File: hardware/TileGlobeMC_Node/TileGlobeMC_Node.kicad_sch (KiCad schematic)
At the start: 85 parts, among them J1 Conn_01x05, J10 LCD, J2 Conn_01x05, J3 Conn_01x05, J4 Conn_01x05, J5 Conn_01x05, J6 Conn_01x05, J7 Conn_01x05, J8 Conn_01x05, J9 SWD, Q1 2N7002, Q2 2N7002, U1 RP2350_80QFN, U2 TPS62A01DRL, U3 BQ24232RGT, U4 ESP-PSRAM64H, U5 PY25Q128HA-WXH, U6 PY25Q128HA-SSH, U7 74AHC1G04, U8 74AHC1G32, Y1 12M

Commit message: Commit before switching to multi board design
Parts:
- removed U8: 74AHC1G32, Package_TO_SOT_SMD:SOT-23-5, symbol 74xGxx:74AHC1G32
- added C29, C30, C31, C32, C33, C34: 100n, Capacitor_SMD:C_0402_1005Metric, symbol Device:C_Small
- added D1, D2, D4: 1N4148WT, Diode_SMD:D_SOD-523, symbol Diode:1N4148WT
- added D3, D5: 3V, Diode_SMD:D_SOD-523, symbol Device:D_Zener_Small
- added J11: USB_C, Connector_USB:USB_C_Receptacle_GCT_USB4105-xx-A_16P_TopMnt_Horizontal, symbol Connector:USB_C_Receptacle_USB2.0_16P
- added R32, R33: 5.1k, Capacitor_SMD:C_0402_1005Metric, symbol Device:R_Small
- added R34: 100k, Capacitor_SMD:C_0402_1005Metric, symbol Device:R_Small
- added R35, R36, R37, R38, R39, R40, R41: 10k, Capacitor_SMD:C_0402_1005Metric, symbol Device:R_Small
- added SW1, SW2, SW3, SW4, SW5: Left, Button_Switch_SMD:SW_SPST_PTS647_Sx38, symbol Switch:SW_Push
- added U8: SC7A20, Package_LGA:LGA-12_2x2mm_P0.5mm, symbol Sensor_Motion:SC7A20
- J2, J4, J6, J8: value Conn_01x05 -> P_Male; footprint (none) -> Project:BC-15-5P380; symbol Connector_Generic:Conn_01x05 -> Connector_Generic_MountingPin:Conn_01x05_MountingPin
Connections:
- net +5V is gone; now on net VIN: J1.5 (Pin_5), J2.1 (Pin_1), J3.5 (Pin_5), J4.1 (Pin_1), J5.5 (Pin_5), J6.1 (Pin_1), J7.5 (Pin_5), J8.1 (Pin_1)
- net +3V3: now also C29.1, R36.2, R37.2, SW2.2, SW3.2, SW4.2, SW5.2, U8.3 (VDDIO), U8.7 (VDD)
- net 3V3_EN_LATCH: now also D4.2 (A)
- net GND: now also J2.MP (MountPin), J4.MP (MountPin), J6.MP (MountPin), J8.MP (MountPin), C29.2, C30.2, C31.2, C32.2, C33.2, C34.2, D3.2 (A), D5.2 (A), J11.A1 (GND), J11.A12 (GND), J11.B1 (GND), J11.B12 (GND), J11.S1 (SHIELD), R32.1, R33.1, R34.1, U8.4 (NC), U8.8 (GNDIO), U8.9 (GND)
- net USB_D+: now also J11.A6 (D+), J11.B6 (D+)
- net USB_D-: now also J11.A7 (D-), J11.B7 (D-)
- net VBUS: now also SW1.2
- net VIN: now also J11.A4 (VBUS), J11.A9 (VBUS), J11.B4 (VBUS), J11.B9 (VBUS)
- net VIN_PGOOD: now also D2.2 (A)
- net at R23.2: now also D5.1 (K)
- net 3V3_EN: no longer names the net of U2.4 (EN)
- net 3V3_EN: now also D1.1 (K), D2.1 (K), D4.1 (K), R34.2
- net BAT_ISET_SAMPLE renamed BAT_ICHG_SAMPLE
- net VIN_~{PGOOD}: no longer names the net of R22.2, U3.7 (PGOOD), U7.2
- new net: R38.1, SW2.1
- new net: J11.A5 (CC1), R33.2
- new net: J11.B5 (CC2), R32.2
- new net: R41.1, SW5.1
- new net: R39.1, SW3.1
- new net: R40.1, SW4.1
- new net BTN_BOTTOM: C32.1, R39.2
- new net BTN_CENTER: C30.1, D3.1 (K), R35.2
- new net BTN_CENTER_VBUS: D1.2 (A), R35.1, SW1.1
- new net BTN_LEFT: C31.1, R38.2
- new net BTN_RIGHT: C33.1, R40.2
- new net BTN_TOP: C34.1, R41.2
- new net I2C_SCL: U8.12 (SCx)
- new net I2C_SDA: U8.2 (SDx)
- no-connect marks 3 -> 10
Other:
- added sheet Core (Core.kicad_sch)
- added sheet Peripheral (Peripheral.kicad_sch)
- added sheet Power (Power.kicad_sch)
- note added: "3.3V DC-DC"
- note added: "Battery Charger & Power Path"
- note added: "Buttons"
- note added: "Flash & PSRAM"
- note added: "IMU"
- note added: "LCD"
- note added: "Node Ports"
- note added: "Note: buttons use MCU's internal pull-down."
- note added: "TODO: change setting resistors now that we're using bigger batteries"
- note added: "USB-C"
- moved on the sheet: BT1, C25, C26, C27, C28, C4, C5, C7, C8, J1, J10, J3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

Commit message: PCB progress
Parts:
- removed BT1: LIR2032, symbol Device:Battery_Cell
- removed C1, C12, C2, C27, C3, C4, C5, C6, C7, C9: 4.7u, Capacitor_SMD:C_0402_1005Metric, symbol Device:C_Small
- removed C10, C11, C13, C14, C15, C16, C17, C18, C19, C20, C21, C22, C25, C26, C28, C29, C30, C31, C32, C33, C34: 100n, Capacitor_SMD:C_0402_1005Metric, symbol Device:C_Small
- removed C23, C24: 15p, Capacitor_SMD:C_0402_1005Metric, symbol Device:C_Small
- removed C8: 22u, Capacitor_SMD:C_0603_1608Metric, symbol Device:C_Small
- removed D1, D2, D4: 1N4148WT, Diode_SMD:D_SOD-523, symbol Diode:1N4148WT
- removed D3, D5: 3V, Diode_SMD:D_SOD-523, symbol Device:D_Zener_Small
- removed J1, J3, J5, J7: Conn_01x05, symbol Connector_Generic:Conn_01x05
- removed J10: LCD, Connector_FFC-FPC:TE_1-1734839-2_1x12-1MP_P0.5mm_Horizontal, symbol Connector_Generic_MountingPin:Conn_01x12_MountingPin
- removed J11: USB_C, Connector_USB:USB_C_Receptacle_GCT_USB4105-xx-A_16P_TopMnt_Horizontal, symbol Connector:USB_C_Receptacle_USB2.0_16P
- removed J2, J4, J6, J8: P_Male, Project:BC-15-5P380, symbol Connector_Generic_MountingPin:Conn_01x05_MountingPin
- removed J9: SWD, Connector_JST:JST_SH_BM03B-SRSS-TB_1x03-1MP_P1.00mm_Vertical, symbol Connector_Generic_MountingPin:Conn_01x03_MountingPin
- removed JP1: RESET, TestPoint:TestPoint_2Pads_Pitch2.54mm_Drill0.8mm, symbol Jumper:Jumper_2_Small_Open
- removed JP2: USB_BOOT, TestPoint:TestPoint_2Pads_Pitch2.54mm_Drill0.8mm, symbol Jumper:Jumper_2_Small_Open
- removed L1: 3.3u, RP2350:L_pol_2016, symbol Project:L_Polarized_Ferrite_Small
- removed L2: 1u, Inductor_SMD:L_Wuerth_MAPI-2010, symbol Device:L_Ferrite_Small
- removed Q1, Q2: 2N7002, Package_TO_SOT_SMD:SOT-23, symbol Transistor_FET:2N7002
- removed R1, R10, R4, R7: 300, Capacitor_SMD:C_0402_1005Metric, symbol Device:R_Small
- removed R11, R12, R2, R3, R5, R6, R8, R9: 270, Capacitor_SMD:C_0402_1005Metric, symbol Device:R_Small
- removed R13, R24: 33, Capacitor_SMD:C_0402_1005Metric, symbol Device:R_Small
- removed R14, R35, R36, R37, R38, R39, R40, R41: 10k, Capacitor_SMD:C_0402_1005Metric, symbol Device:R_Small
- removed R15: 17.4k, Capacitor_SMD:C_0402_1005Metric, symbol Device:R_Small
- removed R16: 1.5k, Capacitor_SMD:C_0402_1005Metric, symbol Device:R_Small
- removed R17, R18, R19, R22, R23, R28, R29, R34: 100k, Capacitor_SMD:C_0402_1005Metric, symbol Device:R_Small
- removed R20: 86.6k, Capacitor_SMD:C_0402_1005Metric, symbol Device:R_Small
- removed R21: 390k, Capacitor_SMD:C_0402_1005Metric, symbol Device:R_Small
- removed R25, R30: 1k, Capacitor_SMD:C_0402_1005Metric, symbol Device:R_Small
- removed R26, R27: 27, Capacitor_SMD:C_0402_1005Metric, symbol Device:R_Small
- removed R31: 4.7, Capacitor_SMD:C_0402_1005Metric, symbol Device:R_Small
- removed R32, R33: 5.1k, Capacitor_SMD:C_0402_1005Metric, symbol Device:R_Small
- removed SW1, SW2, SW3, SW4, SW5: Left, Button_Switch_SMD:SW_SPST_PTS647_Sx38, symbol Switch:SW_Push
- removed U1: RP2350_80QFN, RP2350:RP2350-QFN-80-1EP_10x10_P0.4mm_EP3.4x3.4mm_ThermalVias, symbol RP2350:RP2350_80QFN
- removed U2: TPS62A01DRL, Package_TO_SOT_SMD:SOT-563, symbol Regulator_Switching:TPS62A01DRL
- removed U3: BQ24232RGT, Package_DFN_QFN:VQFN-16-1EP_3x3mm_P0.5mm_EP1.68x1.68mm_ThermalVias, symbol Project:BQ24232RGT
- removed U4: ESP-PSRAM64H, Package_SO:SOIC-8_3.9x4.9mm_P1.27mm, symbol Project:ESP-PSRAM64
- removed U5: PY25Q128HA-WXH, Package_SON:WSON-8-1EP_6x5mm_P1.27mm_EP3.4x4.3mm, symbol Memory_Flash:W25Q128JVP
- removed U6: PY25Q128HA-SSH, Package_SO:SOIC-8_5.3x5.3mm_P1.27mm, symbol Memory_Flash:W25Q128JVS
- removed U7: 74AHC1G04, Package_TO_SOT_SMD:SOT-23-5, symbol 74xGxx:74AHC1G04
- removed U8: SC7A20, Package_LGA:LGA-12_2x2mm_P0.5mm, symbol Sensor_Motion:SC7A20
- removed Y1: 12M, Crystal:Crystal_SMD_3225-4Pin_3.2x2.5mm, symbol Device:Crystal_GND24
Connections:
- no-connect marks 10 -> 29
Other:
- removed sheet Power
- sheet Core ports: added +3V3, BTN_CENTER, BTN_CENTER_VBUS, GND_CORE, GPIO0, GPIO1, GPIO2, GPIO3, GPIO4, I2C_SCL, I2C_SDA, LCD_CS, LCD_DC, LCD_MOSI, LCD_SCK, PERI_INT, VBUS; removed none
- sheet Peripheral ports: added +3V3, BTN_CENTER, BTN_CENTER_VBUS, GND_PERI, I2C_SCL, I2C_SDA, LCD_CS, LCD_DC, LCD_MOSI, LCD_SCK, PERI_INT, VBUS; removed none
- note removed: "3.3V DC-DC"
- note removed: "Battery Charger & Power Path"
- note removed: "Buttons"
- note removed: "Flash & PSRAM"
- note removed: "IMU"
- note removed: "LCD"
- note removed: "Node Ports"
- note removed: "Note: buttons use MCU's internal pull-down."
- note removed: "TODO: change setting resistors now that we're using bigger batteries"
- note removed: "USB-C"

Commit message: PCB progress
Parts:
- added J20: Conn_01x24_MountingPin, Project:FPC_Verticle_24pin_0.5mm, symbol Connector_Generic_MountingPin:Conn_01x24_MountingPin
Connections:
- no-connect marks 29 -> 35
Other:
- sheet Core ports: added GPIO10, GPIO11, GPIO12, GPIO5, GPIO6, GPIO7, GPIO8, GPIO9, USB_D+, USB_D-, VIN; removed BTN_CENTER, I2C_SCL, I2C_SDA, LCD_CS, LCD_DC, LCD_MOSI, LCD_SCK, PERI_INT
- sheet Peripheral ports: added USB_D+, USB_D-, VIN; removed none

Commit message: Main PCB progress
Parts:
- added J21: Conn_01x24_MountingPin, Project:FPC_Verticle_24pin_0.5mm, symbol Connector_Generic_MountingPin:Conn_01x24_MountingPin
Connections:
- net Core/BTN_CENTER_VBUS: now also J20.23 (Pin_23)
- net Core/GPIO0: now also J20.19 (Pin_19)
- net Core/GPIO1: now also J20.18 (Pin_18)
- net Core/GPIO10: now also J20.9 (Pin_9)
- net Core/GPIO11: now also J20.8 (Pin_8)
- net Core/GPIO12: now also J20.7 (Pin_7)
- net Core/GPIO2: now also J20.17 (Pin_17)
- net Core/GPIO3: now also J20.16 (Pin_16)
- net Core/GPIO4: now also J20.15 (Pin_15)
- net Core/GPIO5: now also J20.14 (Pin_14)
- net Core/GPIO6: now also J20.13 (Pin_13)
- net Core/GPIO7: now also J20.12 (Pin_12)
- net Core/GPIO8: now also J20.11 (Pin_11)
- net Core/GPIO9: now also J20.10 (Pin_10)
- net Core/USB_D+: now also J20.3 (Pin_3)
- net Core/USB_D-: now also J20.2 (Pin_2)
- net Core/VBUS: now also J20.22 (Pin_22)
- net Core/VIN: now also J20.20 (Pin_20), J20.21 (Pin_21)
- net Peripheral/BTN_CENTER_VBUS: now also J21.23 (Pin_23)
- net Peripheral/VBUS: now also J21.22 (Pin_22)
- net Peripheral/VIN: now also J21.20 (Pin_20), J21.21 (Pin_21)
- net GND_CORE: now reaches J20.1 (Pin_1)
- net GND_CORE: now also J20.24 (Pin_24), J20.MP (MountPin)
- new net GND_PERI: J21.1 (Pin_1), J21.24 (Pin_24), J21.MP (MountPin)
- no-connect marks 35 -> 14
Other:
- moved on the sheet: J20

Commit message: Main PCB done
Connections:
- net Core/+3V3: now also J20.5 (Pin_5)
- net GND_CORE: now also J20.4 (Pin_4), J20.6 (Pin_6)
- net GND_PERI: now also J21.4 (Pin_4), J21.6 (Pin_6)
- net Peripheral/+3V3: now also J21.5 (Pin_5)
- net Peripheral/USB_D+: now also J21.3 (Pin_3)
- net Peripheral/USB_D-: now also J21.2 (Pin_2)
- no-connect marks 14 -> 0

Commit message: PCB done
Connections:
- net Peripheral/BTN_CENTER: now also J21.8 (Pin_8)
- net Peripheral/I2C_SCL: now also J21.13 (Pin_13)
- net Peripheral/I2C_SDA: now also J21.14 (Pin_14)
- net Peripheral/LCD_CS: now also J21.19 (Pin_19)
- net Peripheral/LCD_DC: now also J21.16 (Pin_16)
- net Peripheral/LCD_MOSI: now also J21.17 (Pin_17)
- net Peripheral/LCD_SCK: now also J21.18 (Pin_18)
- net Peripheral/PERI_INT: now also J21.15 (Pin_15)
- no-connect marks 0 -> 5
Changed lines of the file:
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@@
 		(color 0 0 0 0)
 	)
+	(no_connect
+		(at 182.88 101.6)
+	)
+	(no_connect
+		(at 182.88 99.06)
+	)
+	(no_connect
+		(at 182.88 93.98)
+	)
+	(no_connect
+		(at 182.88 106.68)
+	)
+	(no_connect
+		(at 182.88 104.14)
+	)
 	(wire
 		(pts
@@
 	(wire
 		(pts
+			(xy 182.88 124.46) (xy 187.96 124.46)
+		)
+		(stroke
+			(width 0)
+			(type default)
+		)
+	)
+	(wire
+		(pts
 			(xy 162.56 109.22) (xy 167.64 109.22)
 		)
@@
 	(wire
 		(pts
+			(xy 182.88 121.92) (xy 187.96 121.92)
+		)
+		(stroke
+			(width 0)
+			(type default)
+		)
+	)
+	(wire
+		(pts
 			(xy 162.56 81.28) (xy 167.64 81.28)
 		)
@@
 	(wire
 		(pts
+			(xy 182.88 119.38) (xy 187.96 119.38)
+		)
+		(stroke
+			(width 0)
+			(type default)
+		)
+	)
+	(wire
+		(pts
 			(xy 182.88 129.54) (xy 187.96 129.54)
 		)
@@
 	(wire
 		(pts
+			(xy 182.88 96.52) (xy 187.96 96.52)
+		)
+		(stroke
+			(width 0)
+			(type default)
+		)
+	)
+	(wire
+		(pts
 			(xy 162.56 124.46) (xy 167.64 124.46)
 		)
@@
 	(wire
 		(pts
+			(xy 182.88 109.22) (xy 187.96 109.22)
+		)
+		(stroke
+			(width 0)
+			(type default)
+		)
+	)
+	(wire
+		(pts
 			(xy 162.56 104.14) (xy 167.64 104.14)
 		)
@@
 	(wire
 		(pts
+			(xy 182.88 114.3) (xy 187.96 114.3)
+		)
+		(stroke
+			(width 0)
+			(type default)
+		)
+	)
+	(wire
+		(pts
 			(xy 162.56 119.38) (xy 167.64 119.38)
 		)
@@
 	(wire
 		(pts
+			(xy 182.88 116.84) (xy 187.96 116.84)
+		)
+		(stroke
+			(width 0)
+			(type default)
+		)
+	)
+	(wire
+		(pts
 			(xy 162.56 111.76) (xy 167.64 111.76)
+		)
+		(stroke
+			(width 0)
+			(type default)
+		)
+	)
+	(wire
+		(pts
+			(xy 182.88 111.76) (xy 187.96 111.76)
 		)
 		(stroke
@@
 		)
 		(pin "BTN_CENTER" output
-			(at 187.96 92.71 180)
+			(at 187.96 96.52 180)
 			(effects
 				(font
@@
 		)
 		(pin "I2C_SCL" input
-			(at 187.96 96.52 180)
+			(at 187.96 109.22 180)
 			(effects
 				(font
@@
 		)
 		(pin "I2C_SDA" bidirectional
-			(at 187.96 99.06 180)
+			(at 187.96 111.76 180)
 			(effects
 				(font
@@
 		)
 		(pin "LCD_CS" input
-			(at 187.96 104.14 180)
+			(at 187.96 124.46 180)
 			(effects
 				(font
@@
 		)
 		(pin "LCD_DC" input
-			(at 187.96 106.68 180)
+			(at 187.96 116.84 180)
 			(effects
 				(font
@@
 		)
 		(pin "LCD_MOSI" input
-			(at 187.96 110.49 180)
+			(at 187.96 119.38 180)
 			(effects
 				(font
@@
 		)
 		(pin "LCD_SCK" input
-			(at 187.96 113.03 180)
+			(at 187.96 121.92 180)
 			(effects
 				(font
@@
 		)
 		(pin "PERI_INT" output
-			(at 187.96 118.11 180)
-			(effects
-				(font
+			(at 187.96 114.3 180)
+			(effects
+				(font

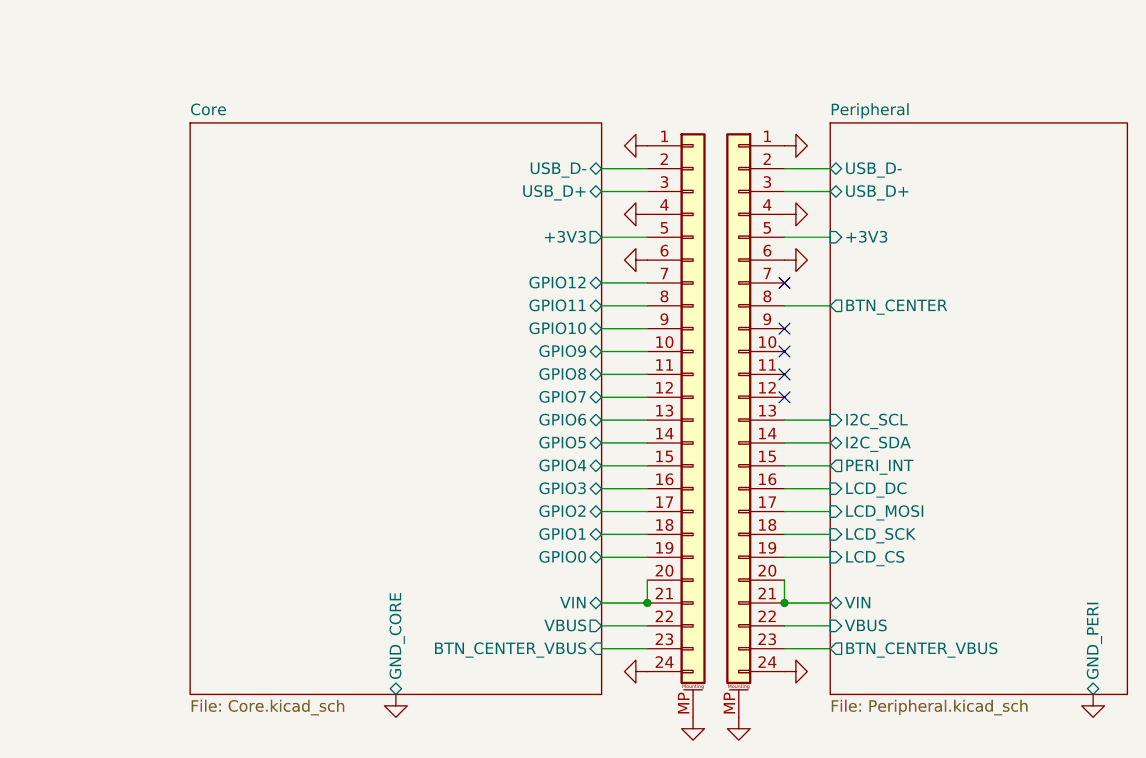
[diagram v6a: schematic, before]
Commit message: BOM; PCB minor tweaks
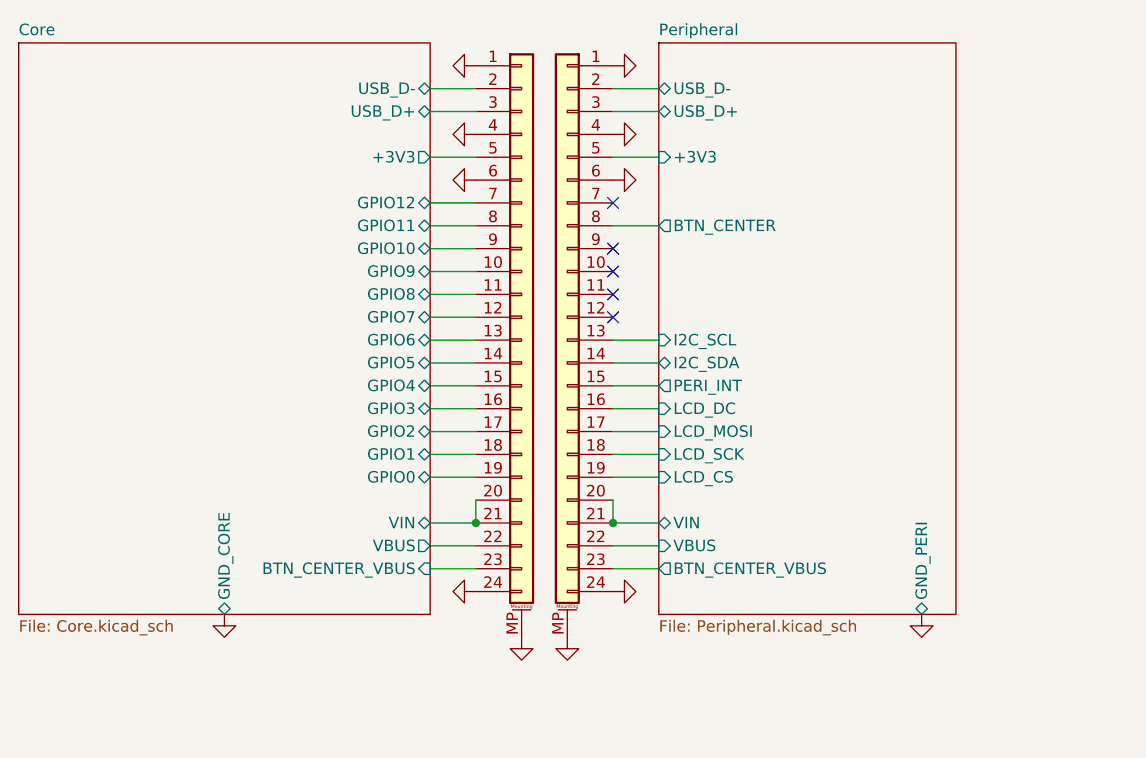
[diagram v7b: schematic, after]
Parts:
- J20, J21: Link (none) -> https://www.lcsc.com/product-detail/C49274051.html
